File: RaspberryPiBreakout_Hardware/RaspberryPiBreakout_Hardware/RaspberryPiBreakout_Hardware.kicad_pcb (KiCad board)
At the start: 2 copper layers, 124.5 x 79.2 mm, 23 parts, among them U1 OKI, U2 Raspberry_Pi, U3 OKI

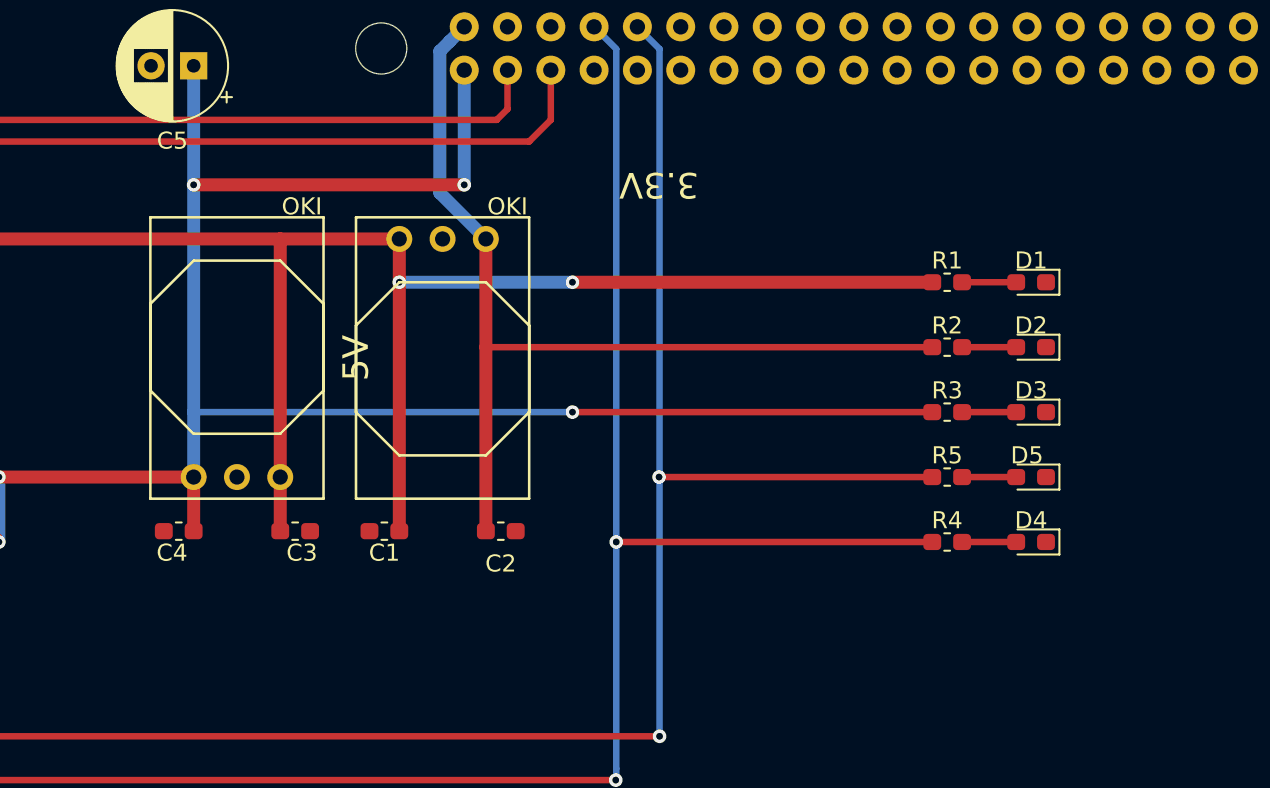
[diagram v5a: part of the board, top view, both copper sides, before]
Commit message: added 2 new leds
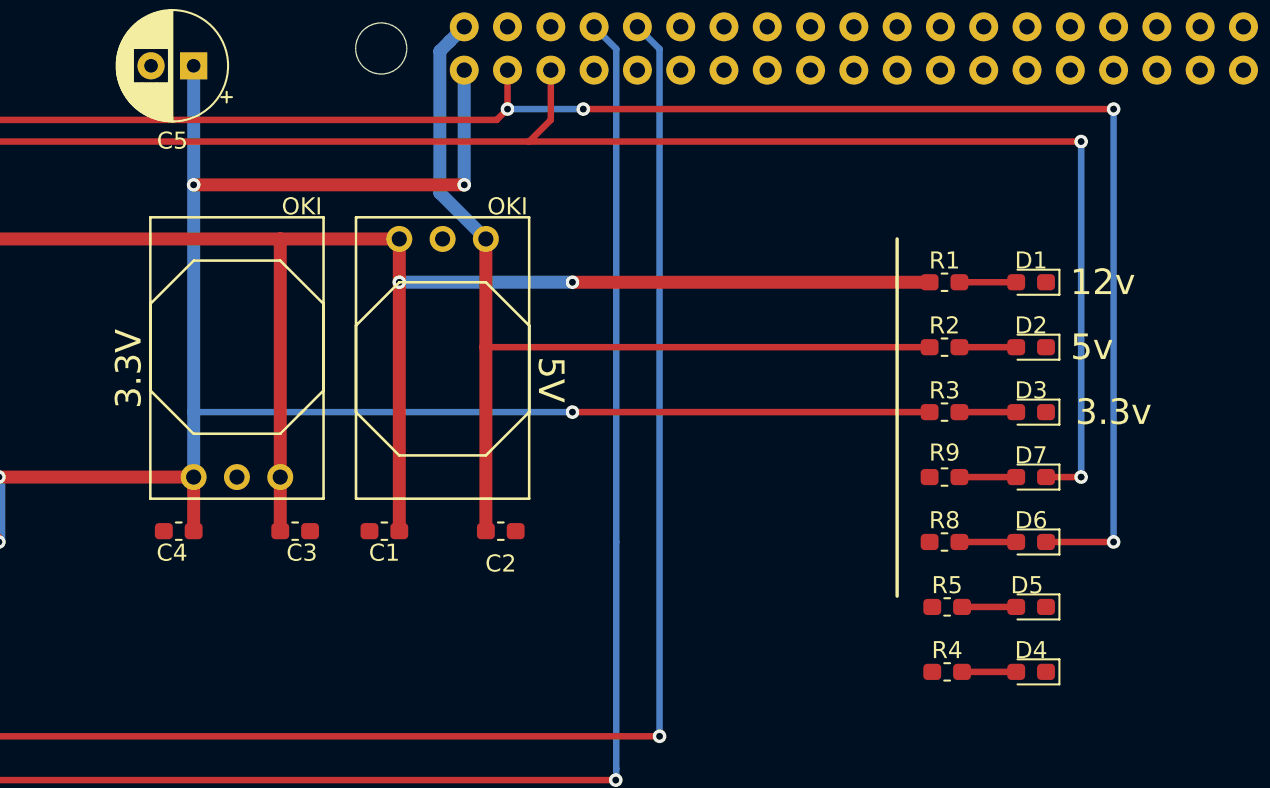
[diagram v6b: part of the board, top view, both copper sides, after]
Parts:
- added D6: LED, Diode_SMD:D_0603_1608Metric_Pad1.05x0.95mm_HandSolder, F.Cu at (156.4, 106.7)
- added D7: LED, Diode_SMD:D_0603_1608Metric_Pad1.05x0.95mm_HandSolder, F.Cu at (156.4, 102.9)
- added R8: 500, Resistor_SMD:R_0603_1608Metric_Pad1.05x0.95mm_HandSolder, F.Cu at (151.4, 106.7)
- added R9: 500, Resistor_SMD:R_0603_1608Metric_Pad1.05x0.95mm_HandSolder, F.Cu at (151.4, 102.9)
- R1: value 500 -> 1k
- moved D4 7.62 mm to (156.4, 114.3)
- moved D5 7.62 mm to (156.4, 110.5)
- moved R4 7.62 mm to (151.5, 114.3)
- moved R5 7.62 mm to (151.5, 110.5)
- moved R1 0.16 mm to (151.4, 91.4)
- moved R2 0.16 mm to (151.4, 95.2)
- moved R3 0.16 mm to (151.4, 99.1)
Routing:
- net SDA1: track 65.0 -> 130.0 mm, vias 2 -> 6
- net SCL1: track 63.4 -> 117.5 mm, vias 2 -> 4
- net Serial_Tx: track 109.0 -> 90.5 mm, vias 2 -> 1
- net Serial_Rx: track 106.5 -> 90.5 mm, vias 2 -> 1
- net Net-(D7-Pad2): track 0.00 -> 3.33 mm
- net Net-(D6-Pad2): track 0.00 -> 3.33 mm
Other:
- board text added: "12v"
- board text added: "3.3v"
- board text added: "5v"

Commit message: added silkscreens
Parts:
- added G***: LOGO, MRDT_Silkscreens:0_MRDT_Logo_20mm, F.Cu at (184.2, 141.0)
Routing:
- net Serial_Tx: track 90.5 -> 109.0 mm, vias 1 -> 2
- net Serial_Rx: track 90.5 -> 106.5 mm, vias 1 -> 2
- net +3V3: track 124.5 -> 132.2 mm, vias 5 -> 3
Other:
- board text added: "LED IND"
- board text added: "RX"
- board text added: "Raspberry Pi Breakout, Rev 2 Mars Rover Design Team Missouri S&T, 2019 Zak Brooks"
- board text added: "SCL"
- board text added: "SDA"
- board text added: "TX"
- board text removed: "Raspberry Pi Breakout, Rev 1 Mars Rover Design Team Missouri S&T, 2019 Andrew Van Horn"
